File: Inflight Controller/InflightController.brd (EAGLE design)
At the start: 74.2 x 58.2 mm, 8 parts

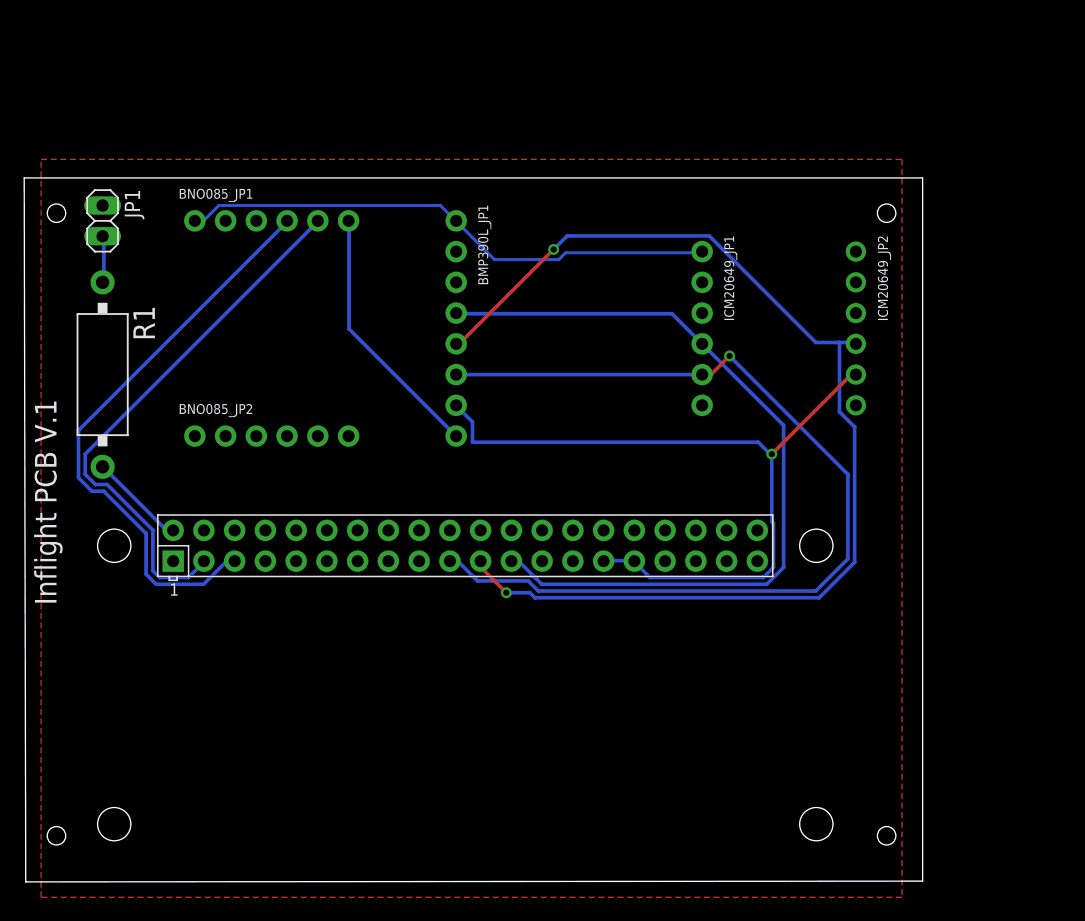
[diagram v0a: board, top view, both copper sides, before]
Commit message: Fixed CS routing error
5/23/21
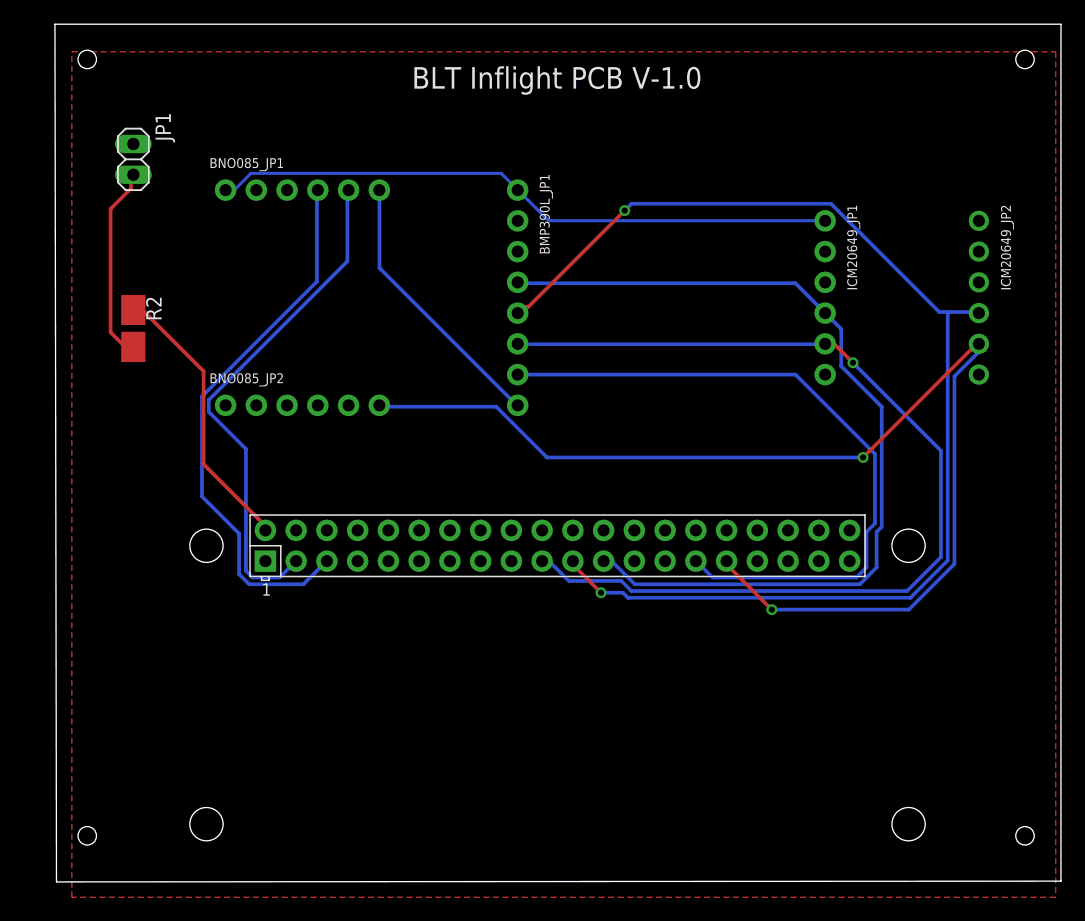
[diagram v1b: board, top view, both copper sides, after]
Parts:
- removed R1: 27, resistor-power:CA0001
- added R2: (no value), resistor-shunt:SMK
- moved ICM20649_JP1 10.5 mm to (63.5, 48.3)
- moved ICM20649_JP2 10.5 mm to (76.2, 48.3)
- moved U$1 7.62 mm to (8.89, 1.27)
- moved BMP390L_JP1 5.68 mm to (38.1, 48.3)
- moved JP1 5.68 mm to (6.35, 59.7)
- moved BNO085_JP1 3.59 mm to (20.3, 57.1)
- moved BNO085_JP2 3.59 mm to (20.3, 39.4)
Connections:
- removed net CS: BMP390L_JP1.7, BNO085_JP2.6, ICM20649_JP2.5, U$1.29, U$1.31
- new net CS_1: BMP390L_JP1.7, U$1.29
- new net CS_2: BNO085_JP2.6, ICM20649_JP2.5, U$1.31
- net 5V0@1: now also R2.2; no longer R1.2
- net N$1: now also R2.1; no longer R1.1
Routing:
- net CS_2: track 0.00 -> 96.6 mm, vias 0 -> 2
- net CS: track 62.9 -> 0.00 mm, vias 1 -> 0
- net CS_1: track 0.00 -> 56.9 mm
- net 5V0@1: track 8.01 -> 23.2 mm
- net N$1: track 3.90 -> 16.2 mm
- net SDO/ADR: track 92.5 -> 99.8 mm
- net VCC: track 44.6 -> 51.8 mm
- net SCK/SCL: track 66.3 -> 73.5 mm
- net SDI/SDA: track 78.9 -> 82.5 mm
- net SCL/SCK/RX: track 47.7 -> 45.4 mm
- net SDA/MISO/TX: track 44.8 -> 42.5 mm
- net INT: track 21.5 -> 22.6 mm
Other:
- board size 74.2 x 58.2 mm -> 83.1 x 70.9 mm
- board text added: "BLT Inflight PCB V-1.0"
- board text removed: "Inflight PCB V.1"

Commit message: Fixed VCC routing from PI
5/24/21
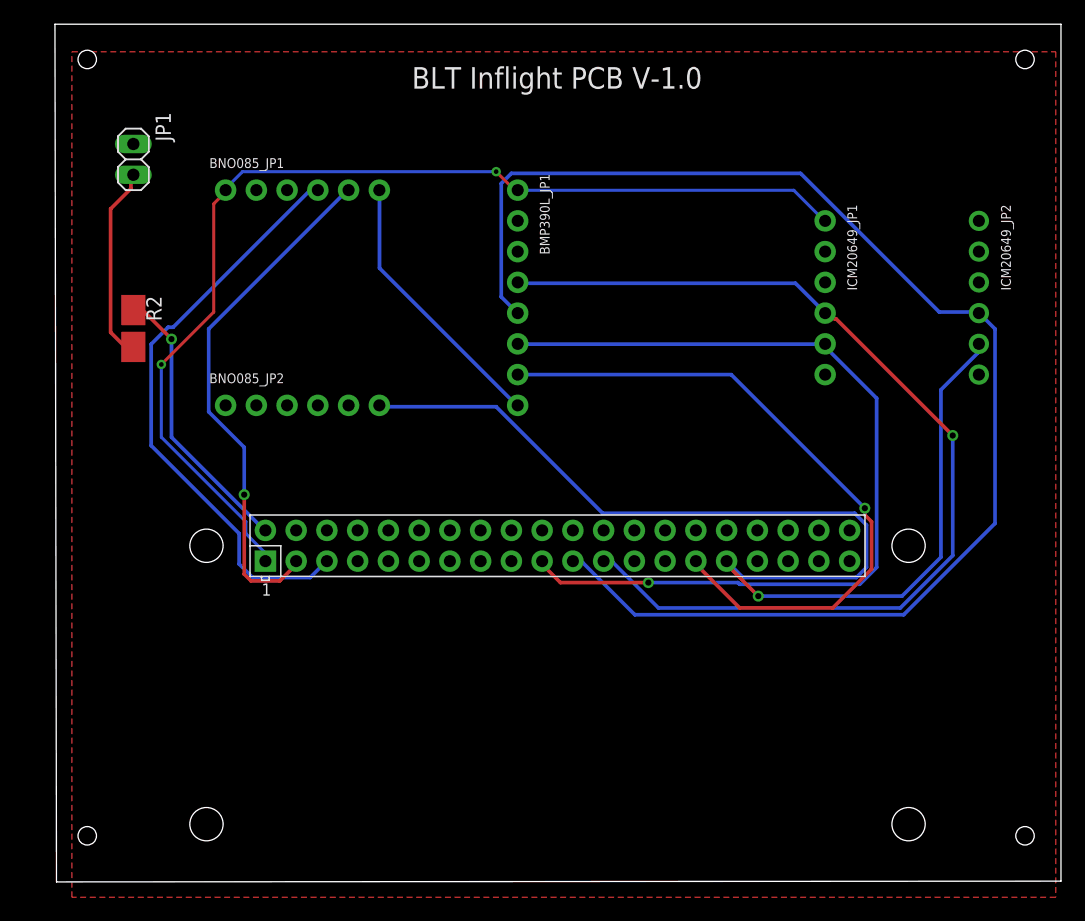
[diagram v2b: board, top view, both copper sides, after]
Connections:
- removed net 3V3@1: U$1.1
- net VCC: now also U$1.1
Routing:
- net VCC: track 51.8 -> 88.3 mm, vias 0 -> 2
- net SDO/ADR: track 99.8 -> 113.6 mm, vias 2 -> 0
- net SCK/SCL: track 73.5 -> 83.4 mm, vias 0 -> 1
- net SDI/SDA: track 82.5 -> 74.9 mm
- net SCL/SCK/RX: track 45.4 -> 48.5 mm
- net CS_2: track 96.6 -> 99.7 mm, vias 2 -> 1
- net CS_1: track 56.9 -> 56.1 mm, vias 0 -> 1
- net SDA/MISO/TX: track 42.5 -> 43.1 mm, vias 0 -> 1
- net 5V0@1: vias 0 -> 1

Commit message: Fixed more traces
5/24/21
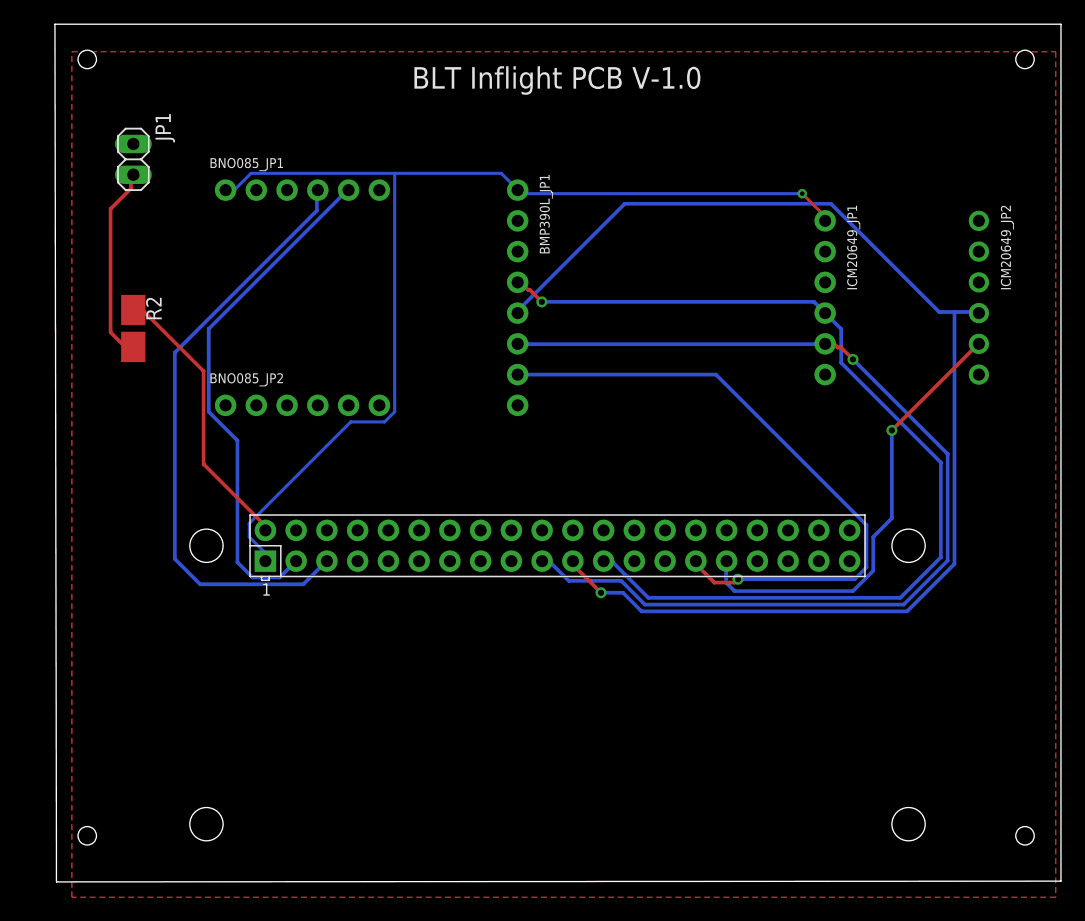
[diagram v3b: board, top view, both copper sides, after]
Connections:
- removed net INT: BMP390L_JP1.8, BNO085_JP1.6
- new net CS_3: BNO085_JP2.6
- new net INT_1: BMP390L_JP1.8
- new net INT_2: BNO085_JP1.6
- net CS_2: no longer BNO085_JP2.6
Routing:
- net CS_2: track 99.7 -> 37.3 mm
- net INT: track 22.6 -> 0.00 mm
- net SDO/ADR: track 113.6 -> 101.6 mm, vias 0 -> 1
- net SDI/SDA: track 74.9 -> 84.6 mm
- net CS_1: track 56.1 -> 53.0 mm
- net VCC: track 88.3 -> 91.3 mm, vias 2 -> 1
- net SCK/SCL: track 83.4 -> 81.1 mm
- net SCL/SCK/RX: track 48.5 -> 49.6 mm
- net SDA/MISO/TX: track 43.1 -> 42.5 mm, vias 1 -> 0
- net 5V0@1: vias 1 -> 0
